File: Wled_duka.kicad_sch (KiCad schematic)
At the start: 42 parts, among them J1 7775-2, J2 DATA channels, J3 CH1&2, J4 CH3&4, J5 Relay out, J6 DMX512, J7 7775-2, J8 Vin_alt, Q1 AO3400A, U1 XL1509-5.0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

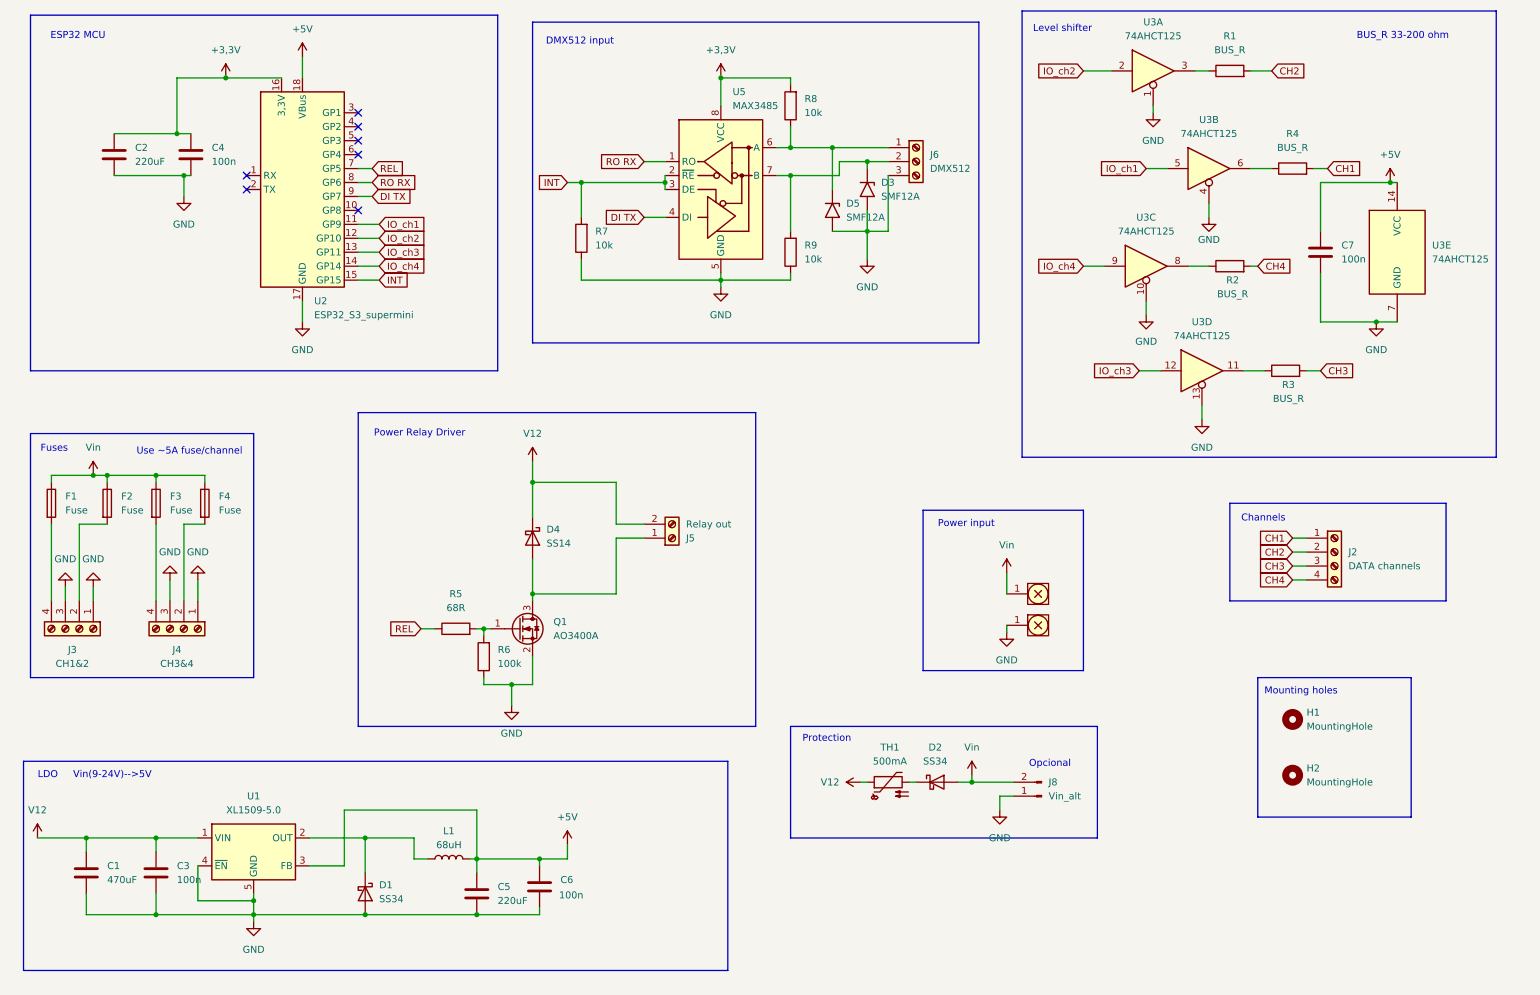
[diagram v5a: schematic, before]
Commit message: Mouser.com ready components
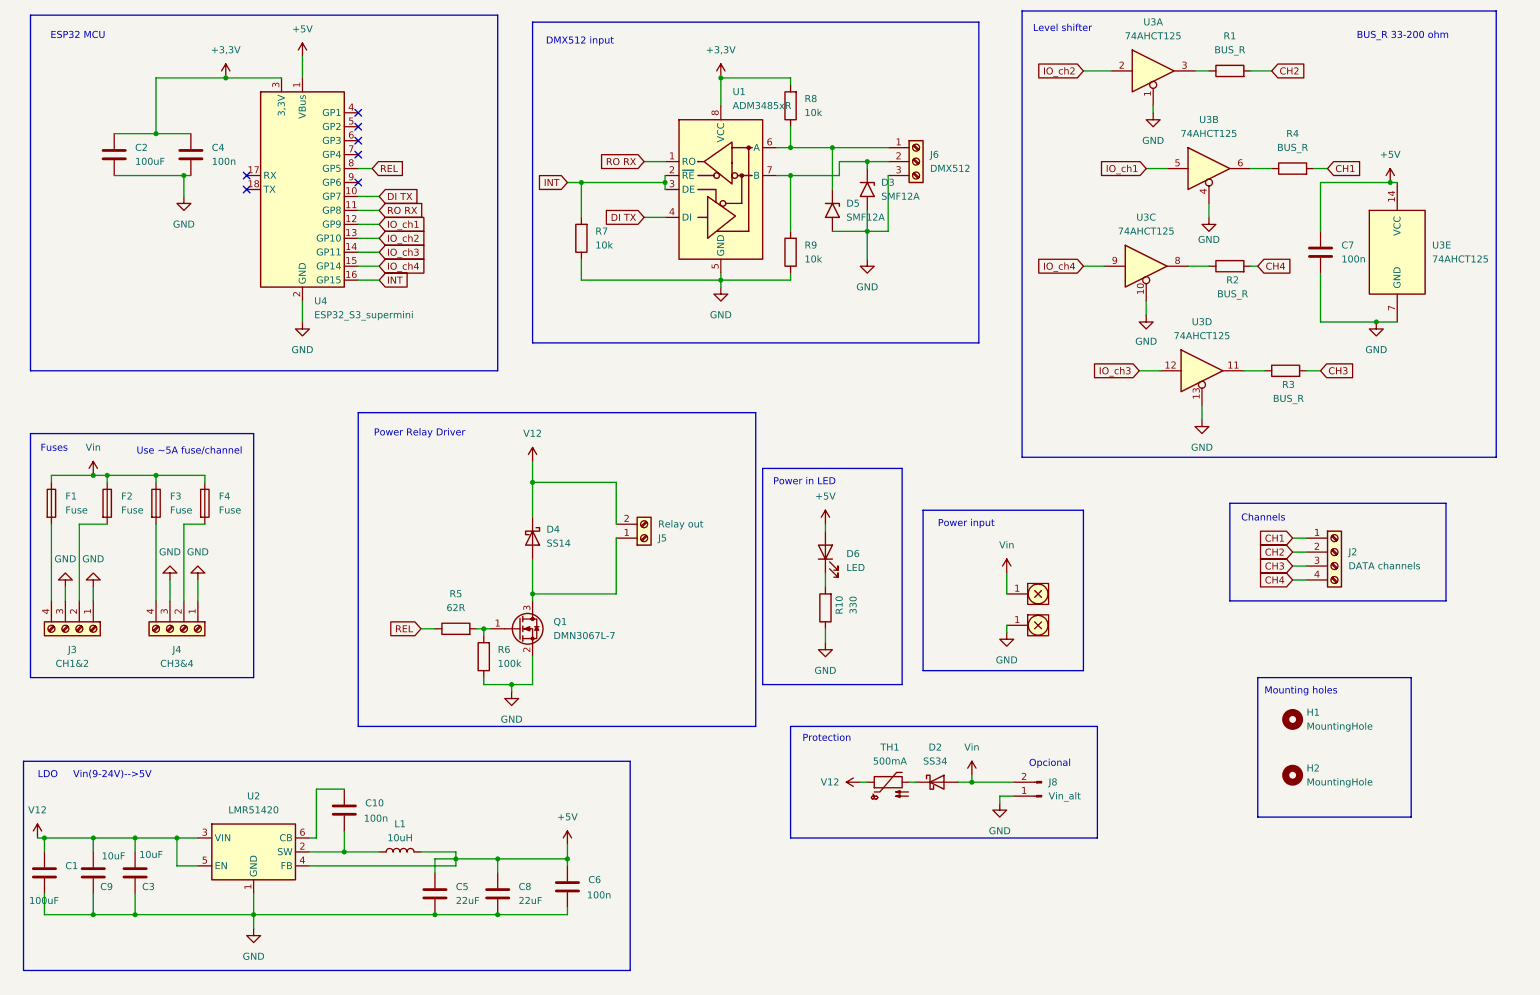
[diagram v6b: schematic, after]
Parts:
- removed D1: SS34, Diode_SMD:D_SMA_Handsoldering, symbol Diode:SS34
- removed Q1: AO3400A, Package_TO_SOT_SMD:SOT-23, symbol Transistor_FET:AO3400A
- removed U1: XL1509-5.0, Package_SO:SOIC-8_3.9x4.9mm_P1.27mm, symbol Regulator_Switching:XL1509-5.0
- removed U2: ESP32_S3_supermini, sajat:ESP32_S3_supermini, symbol ESP32_S3_supermini:ESP32_S3_supermini
- removed U5: MAX3485, Package_SO:SOIC-8_3.9x4.9mm_P1.27mm, symbol Interface_UART:MAX3485
- added C10: 100n, Capacitor_SMD:C_0805_2012Metric_Pad1.18x1.45mm_HandSolder, symbol Device:C
- added C8: 22uF, Capacitor_SMD:C_1210_3225Metric_Pad1.33x2.70mm_HandSolder, symbol Device:C
- added C9: 10uF, Capacitor_SMD:C_0805_2012Metric_Pad1.18x1.45mm_HandSolder, symbol Device:C
- added D6: LED, LED_SMD:LED_0805_2012Metric_Pad1.15x1.40mm_HandSolder, symbol Device:LED
- added Q1: DMN3067L-7, Package_TO_SOT_SMD:SOT-23, symbol Transistor_FET:DMN3051L
- added R10: 330, Resistor_SMD:R_0805_2012Metric_Pad1.20x1.40mm_HandSolder, symbol Device:R
- added U1: ADM3485xR, Package_SO:SOIC-8_3.9x4.9mm_P1.27mm, symbol Interface_UART:ADM3485xR
- added U2: LMR51420, Package_TO_SOT_SMD:SOT-23-6_Handsoldering, symbol Regulator_Switching:LMR51430
- added U4: ESP32_S3_supermini, Library:ESP32_S3_supermini, symbol ESP32_S3_supermini:ESP32_S3_supermini
- C1: value 470uF -> 100uF; footprint Capacitor_THT:C_Radial_D10.0mm_H16.0mm_P5.00mm -> Capacitor_THT:C_Radial_D5.0mm_H11.0mm_P2.00mm; Mouser Part Number (none) -> EEU-FR1C101B
- C2: value 220uF -> 100uF; Mouser Part Number (none) -> EEU-FR1C101B
- C3: value 100n -> 10uF; Mouser Part Number (none) -> 603-AC805KKX7R6BB106
- C4, C6, C7: Mouser Part Number (none) -> 603-AC402KRX7R9BB104
- C5: value 220uF -> 22uF; footprint Capacitor_THT:C_Radial_D5.0mm_H11.0mm_P2.00mm -> Capacitor_SMD:C_1210_3225Metric_Pad1.33x2.70mm_HandSolder; Mouser Part Number (none) -> 603-CC121KKX7R8BB226
- D2: Mouser Part Number (none) -> 821-SS34ALH
- D4: Mouser Part Number (none) -> 821-SS14MH
- J2: Mouser Part Number (none) -> 490-TBL002A3504GY2GY
- J3, J4: Mouser Part Number (none) -> 523-YK4410400000G
- J5: Mouser Part Number (none) -> 179-TB0011-350-02GR
- J6: Mouser Part Number (none) -> 179-TB0011-350-03GR
- J8: now left out of the parts list
- L1: value 68uH -> 10uH; footprint Inductor_SMD:L_Ferrocore_DLG-0504 -> Inductor_SMD:L_Bourns_SRN6045TA; Mouser Part Number (none) -> 652-SRN4018-100M
- R1, R2, R3, R4: Mouser Part Number (none) -> 603-AC0805FR-7W62RL
- R5: value 68R -> 62R; Mouser Part Number (none) -> 603-AC0805FR-7W62RL
- R6: Mouser Part Number (none) -> 603-AC0805FR-07100KL
- R7, R8, R9: Mouser Part Number (none) -> 603-AC0805FR-1010KL
- TH1: footprint Resistor_THT:R_Axial_DIN0204_L3.6mm_D1.6mm_P5.08mm_Vertical -> Resistor_SMD:R_1206_3216Metric_Pad1.30x1.75mm_HandSolder; Mouser Part Number (none) -> MF-NSMF020-2
- U3: Mouser Part Number (none) -> 771-74HCT125D-T
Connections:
- net +3,3V: now also U1.8 (VCC), U4.3 (3,3V)
- net +5V: now also C8.1, D6.2 (A), U2.4 (FB), U4.1 (VBus)
- net DI TX: now also U1.4 (DI), U4.10 (GP7)
- net GND: now also C8.2, C9.1, Q1.2 (S), R10.1, U1.5 (GND), U2.1 (GND), U4.2 (GND)
- net INT: now also U1.2 (~{RE}), U1.3 (DE), U4.16 (GP15)
- net IO_ch1: now also U4.12 (GP9)
- net IO_ch2: now also U4.13 (GP10)
- net IO_ch3: now also U4.14 (GP11)
- net IO_ch4: now also U4.15 (GP14)
- net REL: now also U4.8 (GP5)
- net RO RX: now also U1.1 (RO), U4.11 (GP8)
- net V12: now also C9.2, U2.3 (VIN), U2.5 (EN)
- net at R5.2, R6.2: now also Q1.1 (G)
- net at D3.1 (A1), J6.2 (Pin_2), R9.2: now also U1.7 (B)
- net at L1.1: now also C10.1, U2.2 (SW)
- net at D5.1 (A1), J6.1 (Pin_1), R8.1: now also U1.6 (A)
- net at D4.2 (A), J5.1 (Pin_1): now also Q1.3 (D)
- new net: C10.2, U2.6 (CB)
- new net: D6.1 (K), R10.2
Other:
- note added: "Power in LED"
- moved on the sheet: C1, C3, C5, C6, J5, L1
